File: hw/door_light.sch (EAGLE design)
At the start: 28 parts, among them IC1 TINY13-20SSU, Q1 BSP250, T1 n-mosfet, T2 KP-3216P3C, U1 MC33063ADE4

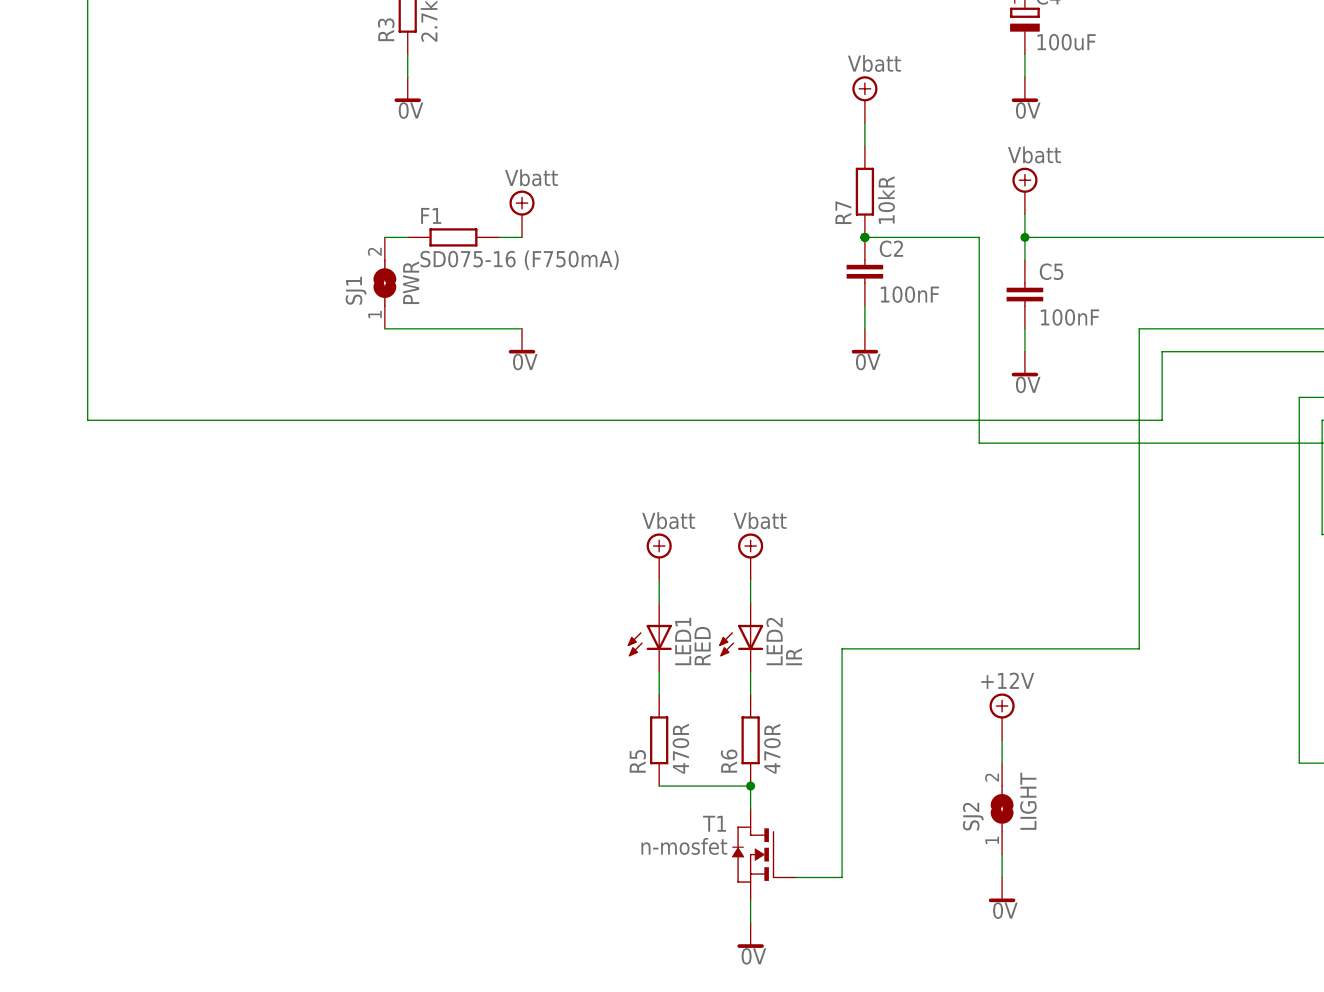
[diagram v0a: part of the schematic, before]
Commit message: added missing R to GND from transistors' gates
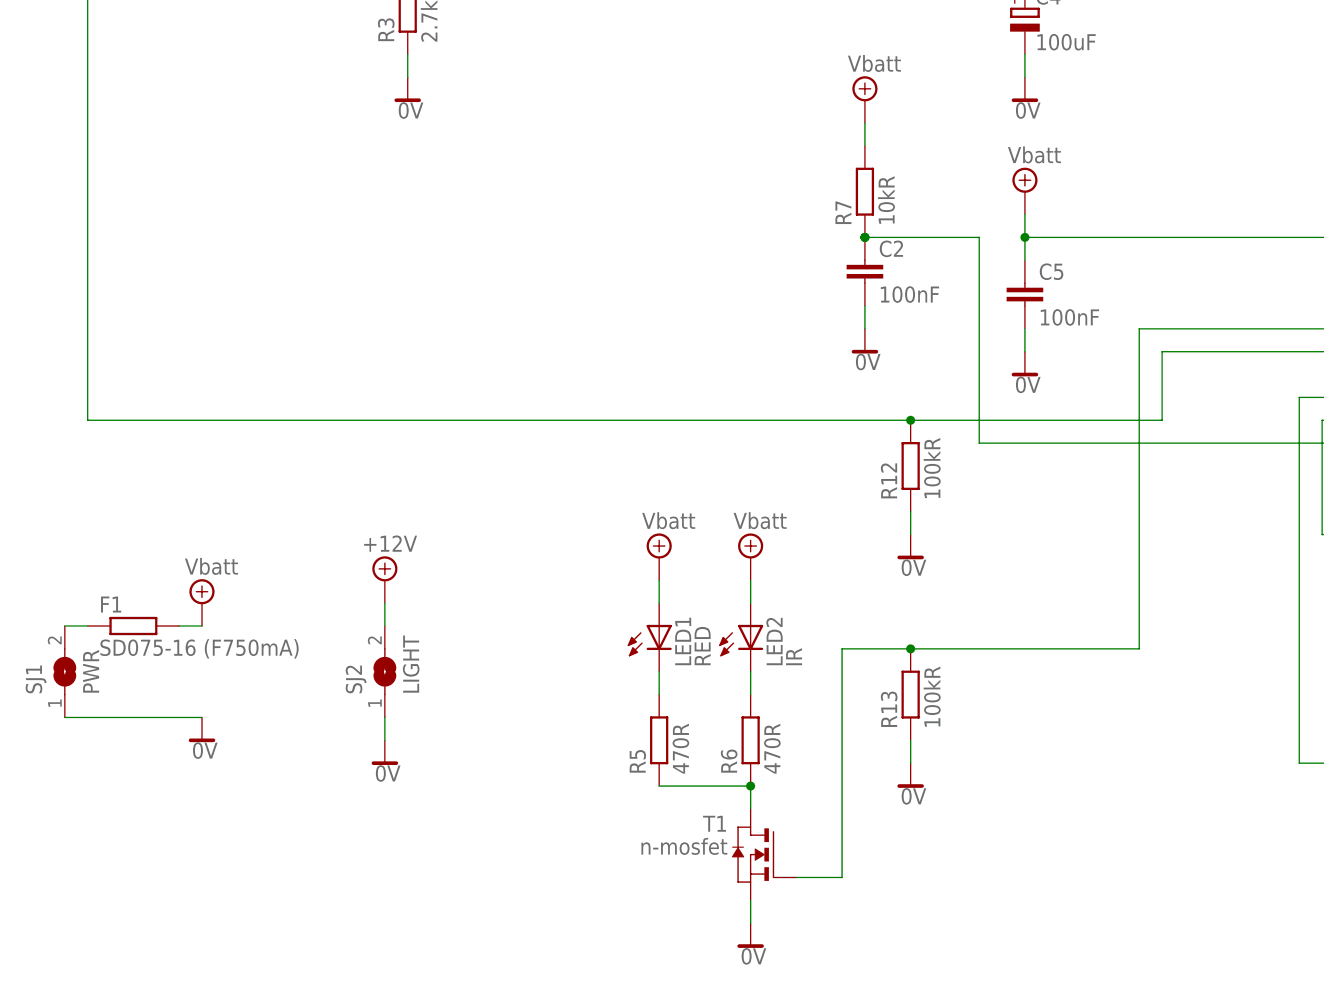
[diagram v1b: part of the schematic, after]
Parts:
- added R12, R13: 100kR, rcl:R-EU_R0603
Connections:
- net 0V: now also R12.1, R13.1
- net N$13: now also R12.2
- net N$14: now also R13.2
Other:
- moved on the sheet: F1, SJ1, SJ2
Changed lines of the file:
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@@
 <part name="SJ1" library="jumper" deviceset="SJ" device="W" value="PWR"/>
 <part name="SJ2" library="jumper" deviceset="SJ" device="W" value="LIGHT"/>
+<part name="R12" library="rcl" deviceset="R-EU_" device="R0603" value="100kR"/>
+<part name="R13" library="rcl" deviceset="R-EU_" device="R0603" value="100kR"/>
+<part name="SUPPLY15" library="supply2" deviceset="0V" device=""/>
+<part name="SUPPLY16" library="supply2" deviceset="0V" device=""/>
 </parts>
 <sheets>
@@
 <instance part="SUPPLY8" gate="0V" x="60.96" y="68.58"/>
 <instance part="SUPPLY10" gate="0V" x="30.48" y="5.08"/>
-<instance part="SUPPLY11" gate="+12V" x="58.42" y="30.48"/>
-<instance part="SUPPLY12" gate="0V" x="58.42" y="10.16"/>
-<instance part="SUPPLY14" gate="0V" x="5.08" y="71.12"/>
+<instance part="SUPPLY11" gate="+12V" x="-10.16" y="45.72"/>
+<instance part="SUPPLY12" gate="0V" x="-10.16" y="25.4"/>
+<instance part="SUPPLY14" gate="0V" x="-30.48" y="27.94"/>
 <instance part="C2" gate="G$1" x="43.18" y="81.28"/>
 <instance part="SUPPLY19" gate="0V" x="43.18" y="71.12"/>
 <instance part="U1" gate="A" x="17.78" y="134.62"/>
-<instance part="SUPPLY26" gate="P" x="5.08" y="86.36"/>
-<instance part="F1" gate="G$1" x="-2.54" y="83.82"/>
+<instance part="SUPPLY26" gate="P" x="-30.48" y="43.18"/>
+<instance part="F1" gate="G$1" x="-38.1" y="40.64"/>
 <instance part="R7" gate="G$1" x="43.18" y="88.9" rot="R90"/>
 <instance part="D1" gate="G$1" x="60.96" y="129.54" rot="R270"/>
@@
 <instance part="Q1" gate="G$1" x="-38.1" y="144.78"/>
 <instance part="T1" gate="A" x="30.48" y="15.24" rot="MR0"/>
-<instance part="SJ1" gate="1" x="-10.16" y="78.74" rot="R90"/>
-<instance part="SJ2" gate="1" x="58.42" y="20.32" rot="R90"/>
+<instance part="SJ1" gate="1" x="-45.72" y="35.56" rot="R90"/>
+<instance part="SJ2" gate="1" x="-10.16" y="35.56" rot="R90"/>
+<instance part="R12" gate="G$1" x="48.26" y="58.42" rot="R90"/>
+<instance part="R13" gate="G$1" x="48.26" y="33.02" rot="R90"/>
+<instance part="SUPPLY15" gate="0V" x="48.26" y="48.26"/>
+<instance part="SUPPLY16" gate="0V" x="48.26" y="22.86"/>
 </instances>
 <busses>
@@
 <pinref part="SJ2" gate="1" pin="1"/>
 <pinref part="SUPPLY12" gate="0V" pin="0V"/>
-<wire x1="58.42" y1="12.7" x2="58.42" y2="15.24" width="0.1524" layer="91"/>
+<wire x1="-10.16" y1="27.94" x2="-10.16" y2="30.48" width="0.1524" layer="91"/>
 </segment>
 <segment>
 <pinref part="SJ1" gate="1" pin="1"/>
 <pinref part="SUPPLY14" gate="0V" pin="0V"/>
-<wire x1="5.08" y1="73.66" x2="-10.16" y2="73.66" width="0.1524" layer="91"/>
+<wire x1="-30.48" y1="30.48" x2="-45.72" y2="30.48" width="0.1524" layer="91"/>
+</segment>
+<segment>
+<pinref part="R12" gate="G$1" pin="1"/>
+<pinref part="SUPPLY15" gate="0V" pin="0V"/>
+<wire x1="48.26" y1="50.8" x2="48.26" y2="53.34" width="0.1524" layer="91"/>
+</segment>
+<segment>
+<pinref part="R13" gate="G$1" pin="1"/>
+<pinref part="SUPPLY16" gate="0V" pin="0V"/>
+<wire x1="48.26" y1="25.4" x2="48.26" y2="27.94" width="0.1524" layer="91"/>
 </segment>
 </net>
@@
 <pinref part="SJ2" gate="1" pin="2"/>
 <pinref part="SUPPLY11" gate="+12V" pin="+12V"/>
-<wire x1="58.42" y1="27.94" x2="58.42" y2="25.4" width="0.1524" layer="91"/>
+<wire x1="-10.16" y1="43.18" x2="-10.16" y2="40.64" width="0.1524" layer="91"/>
 </segment>
 </net>
@@
 <wire x1="-40.64" y1="147.32" x2="-43.18" y2="147.32" width="0.1524" layer="91"/>
 <wire x1="-43.18" y1="147.32" x2="-43.18" y2="63.5" width="0.1524" layer="91"/>
-<wire x1="-43.18" y1="63.5" x2="76.2" y2="63.5" width="0.1524" layer="91"/>
+<wire x1="-43.18" y1="63.5" x2="48.26" y2="63.5" width="0.1524" layer="91"/>
+<wire x1="48.26" y1="63.5" x2="76.2" y2="63.5" width="0.1524" layer="91"/>
 <wire x1="76.2" y1="63.5" x2="76.2" y2="71.12" width="0.1524" layer="91"/>
 <pinref part="Q1" gate="G$1" pin="G"/>
+<pinref part="R12" gate="G$1" pin="2"/>
+<junction x="48.26" y="63.5"/>
 </segment>
 </net>
@@
 <segment>
 <wire x1="73.66" y1="73.66" x2="73.66" y2="38.1" width="0.1524" layer="91"/>
-<wire x1="73.66" y1="38.1" x2="40.64" y2="38.1" width="0.1524" layer="91"/>
+<wire x1="73.66" y1="38.1" x2="48.26" y2="38.1" width="0.1524" layer="91"/>
+<wire x1="48.26" y1="38.1" x2="40.64" y2="38.1" width="0.1524" layer="91"/>
 <wire x1="40.64" y1="38.1" x2="40.64" y2="12.7" width="0.1524" layer="91"/>
 <wire x1="40.64" y1="12.7" x2="35.56" y2="12.7" width="0.1524" layer="91"/>
@@
 <wire x1="99.06" y1="73.66" x2="73.66" y2="73.66" width="0.1524" layer="91"/>
 <pinref part="T1" gate="A" pin="G"/>
+<pinref part="R13" gate="G$1" pin="2"/>
+<junction x="48.26" y="38.1"/>
 </segment>
 </net>
 <net name="+4.1V" class="0">
 <segment>
-<wire x1="5.08" y1="83.82" x2="2.54" y2="83.82" width="0.1524" layer="91"/>
+<wire x1="-30.48" y1="40.64" x2="-33.02" y2="40.64" width="0.1524" layer="91"/>
 <pinref part="SUPPLY26" gate="P" pin="+4.1V"/>
 <pinref part="F1" gate="G$1" pin="2"/>
@@
 <segment>
 <pinref part="F1" gate="G$1" pin="1"/>
-<wire x1="-7.62" y1="83.82" x2="-10.16" y2="83.82" width="0.1524" layer="91"/>
+<wire x1="-43.18" y1="40.64" x2="-45.72" y2="40.64" width="0.1524" layer="91"/>
 <pinref part="SJ1" gate="1" pin="2"/>
 </segment>

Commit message: replaced on-bard big fuse with the smaller one (the one that has been actually bought)
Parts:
- F1: device rcl:R-EU_MELF0207W -> rcl:R-EU_MELF0204W
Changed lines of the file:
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@@
 <part name="U1" library="Texas Instruments_By_element14_Batch_1" deviceset="MC33063ADE4" device=""/>
 <part name="SUPPLY26" library="supply2" deviceset="+4.1V" device="" value="Vbatt"/>
-<part name="F1" library="rcl" deviceset="R-EU_" device="MELF0207W" value="SD075-16 (F750mA)"/>
+<part name="F1" library="rcl" deviceset="R-EU_" device="MELF0204W" value="SD075-16 (F750mA)"/>
 <part name="R7" library="rcl" deviceset="R-EU_" device="R0402" value="10kR"/>
 <part name="D1" library="diode" deviceset="MBRS130LT3" device="" value=" MBRS140T3G"/>
